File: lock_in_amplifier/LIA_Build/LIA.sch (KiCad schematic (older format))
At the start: 28 parts, among them J10 A IN COAX, J11 B IN, J12 POWER_IN, J13 A IN, J14 I IN COAX, J15 I IN, J16 TEST SIGNAL OUT, J18 TEST HIGH SIDE VALUE, J20 AMP OUT, J21 AMP OUT COAX, J22 CLK IN, J23 CLK IN COAX, J26 CLK OUT, J27 CLK OUT COAX, J30 DEMOD OUT - I, J31 DEMOD OUT I COAX, J32 DEMOD OUT Q COAX, J33 DEMOD OUT - Q, J9 B IN COAX

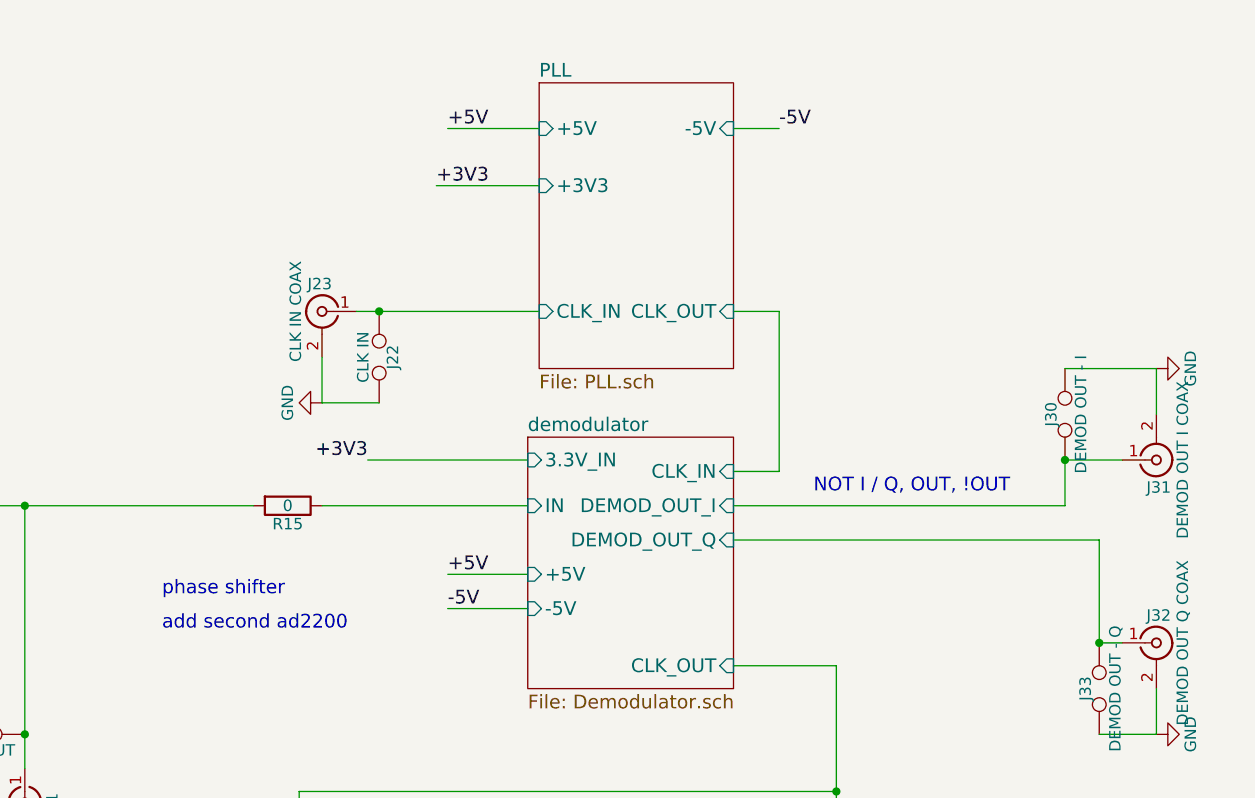
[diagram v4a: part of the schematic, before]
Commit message: Added quadrature demod, phase shift to pll
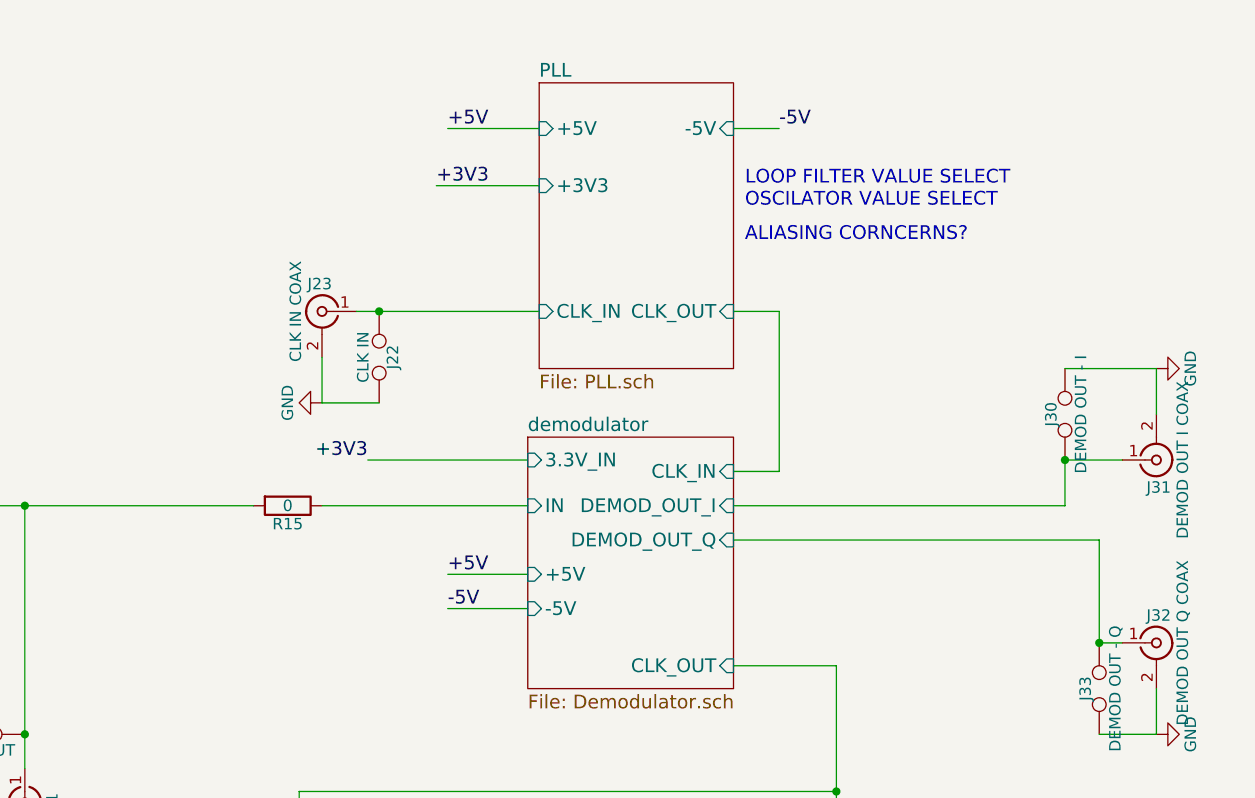
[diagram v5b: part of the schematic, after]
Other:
- note added: "ALIASING CORNCERNS?"
- note added: "LOOP FILTER VALUE SELECT\nOSCILATOR VALUE SELECT"
- note removed: "NOT I / Q, OUT, !OUT"
- note removed: "add second ad2200"
- note removed: "phase shifter"
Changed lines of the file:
@@
 $EndSheet
 $Comp
-L GND #PWR5
+L GND #PWR01
 U 1 1 5A1F9691
 P 2750 3650
-F 0 "#PWR5" H 2750 3400 50  0001 C CNN
+F 0 "#PWR01" H 2750 3400 50  0001 C CNN
 F 1 "GND" H 2750 3500 50  0000 C CNN
 F 2 "" H 2750 3650 50  0001 C CNN
@@
 $EndComp
 $Comp
-L GND #PWR3
+L GND #PWR02
 U 1 1 5A2003C9
 P 1500 2650
-F 0 "#PWR3" H 1500 2400 50  0001 C CNN
+F 0 "#PWR02" H 1500 2400 50  0001 C CNN
 F 1 "GND" H 1500 2500 50  0000 C CNN
 F 2 "" H 1500 2650 50  0001 C CNN
@@
 $EndComp
 $Comp
-L GND #PWR2
+L GND #PWR03
 U 1 1 5A2004F1
 P 1450 4150
-F 0 "#PWR2" H 1450 3900 50  0001 C CNN
+F 0 "#PWR03" H 1450 3900 50  0001 C CNN
 F 1 "GND" H 1450 4000 50  0000 C CNN
 F 2 "" H 1450 4150 50  0001 C CNN
@@
 $EndComp
 $Comp
-L GND #PWR1
+L GND #PWR04
 U 1 1 5A20072D
 P 950 3800
-F 0 "#PWR1" H 950 3550 50  0001 C CNN
+F 0 "#PWR04" H 950 3550 50  0001 C CNN
 F 1 "GND" H 950 3650 50  0000 C CNN
 F 2 "" H 950 3800 50  0001 C CNN
@@
 $EndComp
 $Comp
-L GND #PWR6
+L GND #PWR05
 U 1 1 5A203CBF
 P 4400 5150
-F 0 "#PWR6" H 4400 4900 50  0001 C CNN
+F 0 "#PWR05" H 4400 4900 50  0001 C CNN
 F 1 "GND" H 4400 5000 50  0000 C CNN
 F 2 "" H 4400 5150 50  0001 C CNN
@@
 $EndComp
 $Comp
-L GND #PWR7
+L GND #PWR06
 U 1 1 5A203EC2
 P 6100 3400
-F 0 "#PWR7" H 6100 3150 50  0001 C CNN
+F 0 "#PWR06" H 6100 3150 50  0001 C CNN
 F 1 "GND" H 6100 3250 50  0000 C CNN
 F 2 "" H 6100 3400 50  0001 C CNN
@@
 $EndComp
 $Comp
-L GND #PWR8
+L GND #PWR07
 U 1 1 5A203FFF
 P 7950 5800
-F 0 "#PWR8" H 7950 5550 50  0001 C CNN
+F 0 "#PWR07" H 7950 5550 50  0001 C CNN
 F 1 "GND" H 7950 5650 50  0000 C CNN
 F 2 "" H 7950 5800 50  0001 C CNN
@@
 $EndComp
 $Comp
-L GND #PWR9
+L GND #PWR08
 U 1 1 5A20451A
 P 9750 3250
-F 0 "#PWR9" H 9750 3000 50  0001 C CNN
+F 0 "#PWR08" H 9750 3000 50  0001 C CNN
 F 1 "GND" H 9750 3100 50  0000 C CNN
 F 2 "" H 9750 3250 50  0001 C CNN
@@
 $EndComp
 $Comp
-L GND #PWR10
+L GND #PWR09
 U 1 1 5A204657
 P 9750 4850
-F 0 "#PWR10" H 9750 4600 50  0001 C CNN
+F 0 "#PWR09" H 9750 4600 50  0001 C CNN
 F 1 "GND" H 9750 4700 50  0000 C CNN
 F 2 "" H 9750 4850 50  0001 C CNN
@@
 $EndComp
 $Comp
-L GND #PWR4
+L GND #PWR010
 U 1 1 5A212B2B
 P 1750 6850
-F 0 "#PWR4" H 1750 6600 50  0001 C CNN
+F 0 "#PWR010" H 1750 6600 50  0001 C CNN
 F 1 "GND" H 1750 6700 50  0000 C CNN
 F 2 "" H 1750 6850 50  0001 C CNN
@@
 Text Notes 7250 6600 0    60   ~ 0
 ADD SENSIBLE MCU OUT FOR EVENTUAL MICROCONTROLLER DESIGN
-Text Notes 5400 4250 0    60   ~ 0
-phase shifter
-Text Notes 8250 3800 0    60   ~ 0
-NOT I / Q, OUT, !OUT
-Text Notes 5400 4400 0    60   ~ 0
-add second ad2200
+Text Notes 7950 2550 0    60   ~ 0
+LOOP FILTER VALUE SELECT\nOSCILATOR VALUE SELECT
+Text Notes 7950 2700 0    60   ~ 0
+ALIASING CORNCERNS?
 $EndSCHEMATC

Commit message: pll finalized - misc cleanup - review candidate
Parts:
- added D10, D11, D12, D13, D9: BAT54S, TO_SOT_Packages_SMD:SOT-23, symbol D_Schottky_x2_Serial_AKC
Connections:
- net +3V3: now also D11.2 (K), D12.2 (K), D13.2 (K), D9.2 (K)
- net +5V: now also D10.2 (K)
- net -5V: now also D10.1 (A)
- net GND: now also D11.1 (A), D12.1 (A), D13.1 (A), D9.1 (A)
- net PLL/CLK_IN: now also D10.3 (common)
- net amplifiers/OUT: now also D9.3 (common)
- net demodulator/CLK_OUT: now also D11.3 (common)
- net demodulator/DEMOD_OUT_I: now also D13.3 (common)
- net demodulator/DEMOD_OUT_Q: now also D12.3 (common)
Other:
- note added: "CREATE AN OFFICIAL NOISE BUDGET\nEND TO END NOISE AND GAIN SIM\n"
- note added: "LOOP FILTER VALUE SELECT"
- note removed: "ADD SENSIBLE MCU OUT FOR EVENTUAL MICROCONTROLLER DESIGN"
- note removed: "ALIASING CORNCERNS?"
- note removed: "DFM TODO:\nRESISTOR COMP. CT. MINIMIZATION\nCONSIDER SMALLER PASSIVE PACKAGES (0603 OR 0402)\nMANUFACTURE TP. PLACEMENT.\nMANUFACTURE 0 OHM \nCHEAPER ALT. TO OP1177?\nADD ESD PROTECTION"
- note removed: "LOOP FILTER VALUE SELECT\nOSCILATOR VALUE SELECT"
- note removed: "MAJOR TODO:\nSELECT TRANSIMPEDANCE AMP\nAMPLIFIER NOISE TRADES - WRITEUP / VERIFY\nPLL SELECTION\nLINE FILTER DESIGN"
- note removed: "◦ Work noise budget!\n"
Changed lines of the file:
@@
 F9 "-5V" I L 7000 4300 60
 $EndSheet
-Text Notes 5050 1400 0    60   ~ 0
-	◦	Work noise budget!\n
+Text Notes 8700 800  0    60   ~ 0
+CREATE AN OFFICIAL NOISE BUDGET\nEND TO END NOISE AND GAIN SIM\n
 Text Notes 1650 4550 0    60   ~ 0
 layout notes:\nguard traces around A IN, BIN AND I IN\nlocate near to input connectors\nput 100mil headers under can outline
@@
 Text Notes 5550 6150 2    60   ~ 0
 GUARD TRACES AROUND HIGH IMPEDANCE PATHS
-Text Notes 5150 1200 0    60   ~ 0
-MAJOR TODO:\nSELECT TRANSIMPEDANCE AMP\nAMPLIFIER NOISE TRADES - WRITEUP / VERIFY\nPLL SELECTION\nLINE FILTER DESIGN
-Text Notes 7900 1250 0    60   ~ 0
-DFM TODO:\nRESISTOR COMP. CT. MINIMIZATION\nCONSIDER SMALLER PASSIVE PACKAGES (0603 OR 0402)\nMANUFACTURE TP. PLACEMENT.\nMANUFACTURE 0 OHM \nCHEAPER ALT. TO OP1177?\nADD ESD PROTECTION
 $Comp
 L SPDT S1
@@
 Wire Wire Line
 	6650 4150 7000 4150
-Text Notes 7250 6600 0    60   ~ 0
-ADD SENSIBLE MCU OUT FOR EVENTUAL MICROCONTROLLER DESIGN
 Text Notes 7950 2550 0    60   ~ 0
-LOOP FILTER VALUE SELECT\nOSCILATOR VALUE SELECT
-Text Notes 7950 2700 0    60   ~ 0
-ALIASING CORNCERNS?
+LOOP FILTER VALUE SELECT
+$Comp
+L D_Schottky_x2_Serial_AKC D9
+U 1 1 5A2A8E84
+P 4800 4600
+F 0 "D9" H 4850 4500 50  0000 C CNN
+F 1 "BAT54S" H 4800 4700 50  0000 C CNN
+F 2 "TO_SOT_Packages_SMD:SOT-23" H 4800 4600 50  0001 C CNN
+F 3 "" H 4800 4600 50  0001 C CNN
+	1    4800 4600
+	-1   0    0    1
+$EndComp
+Connection ~ 4800 4400
+$Comp
+L D_Schottky_x2_Serial_AKC D11
+U 1 1 5A2A90E7
+P 8350 4900
+F 0 "D11" H 8400 4800 50  0000 C CNN
+F 1 "BAT54S" H 8350 5000 50  0000 C CNN
+F 2 "TO_SOT_Packages_SMD:SOT-23" H 8350 4900 50  0001 C CNN
+F 3 "" H 8350 4900 50  0001 C CNN
+	1    8350 4900
+	-1   0    0    1
+$EndComp
+Connection ~ 8350 4700
+$Comp
+L D_Schottky_x2_Serial_AKC D12
+U 1 1 5A2A92A3
+P 8400 4000
+F 0 "D12" H 8450 3900 50  0000 C CNN
+F 1 "BAT54S" H 8400 4100 50  0000 C CNN
+F 2 "TO_SOT_Packages_SMD:SOT-23" H 8400 4000 50  0001 C CNN
+F 3 "" H 8400 4000 50  0001 C CNN
+	1    8400 4000
+	0    -1   -1   0
+$EndComp
+$Comp
+L D_Schottky_x2_Serial_AKC D13
+U 1 1 5A2A93F3
+P 8900 3850
+F 0 "D13" H 8950 3750 50  0000 C CNN
+F 1 "BAT54S" H 8900 3950 50  0000 C CNN
+F 2 "TO_SOT_Packages_SMD:SOT-23" H 8900 3850 50  0001 C CNN
+F 3 "" H 8900 3850 50  0001 C CNN
+	1    8900 3850
+	0    -1   -1   0
+$EndComp
+$Comp
+L D_Schottky_x2_Serial_AKC D10
+U 1 1 5A2A952B
+P 6650 3000
+F 0 "D10" H 6700 2900 50  0000 C CNN
+F 1 "BAT54S" H 6650 3100 50  0000 C CNN
+F 2 "TO_SOT_Packages_SMD:SOT-23" H 6650 3000 50  0001 C CNN
+F 3 "" H 6650 3000 50  0001 C CNN
+	1    6650 3000
+	0    -1   -1   0
+$EndComp
+Connection ~ 6850 3000
+$Comp
+L GND #PWR011
+U 1 1 5A2AB5C7
+P 5100 4600
+F 0 "#PWR011" H 5100 4350 50  0001 C CNN
+F 1 "GND" H 5100 4450 50  0000 C CNN
+F 2 "" H 5100 4600 50  0001 C CNN
+F 3 "" H 5100 4600 50  0001 C CNN
+	1    5100 4600
+	1    0    0    -1
+$EndComp
+$Comp
+L GND #PWR012
+U 1 1 5A2AB6F5
+P 8650 4900
+F 0 "#PWR012" H 8650 4650 50  0001 C CNN
+F 1 "GND" H 8650 4750 50  0000 C CNN
+F 2 "" H 8650 4900 50  0001 C CNN
+F 3 "" H 8650 4900 50  0001 C CNN
+	1    8650 4900
+	1    0    0    -1
+$EndComp
+$Comp
+L GND #PWR013
+U 1 1 5A2AB823
+P 8900 4150
+F 0 "#PWR013" H 8900 3900 50  0001 C CNN
+F 1 "GND" H 8900 4000 50  0000 C CNN
+F 2 "" H 8900 4150 50  0001 C CNN
+F 3 "" H 8900 4150 50  0001 C CNN
+	1    8900 4150
+	1    0    0    -1
+$EndComp
+$Comp
+L GND #PWR014
+U 1 1 5A2AB951
+P 8400 4300
+F 0 "#PWR014" H 8400 4050 50  0001 C CNN
+F 1 "GND" H 8400 4150 50  0000 C CNN
+F 2 "" H 8400 4300 50  0001 C CNN
+F 3 "" H 8400 4300 50  0001 C CNN
+	1    8400 4300
+	1    0    0    -1
+$EndComp
+Text Label 4500 4600 2    60   ~ 0
++3V3
+Text Label 8900 3550 2    60   ~ 0
++3V3
+Text Label 8400 3700 2    60   ~ 0
++3V3
+Text Label 8050 4900 2    60   ~ 0
++3V3
+Text Label 6650 2700 0    60   ~ 0
++5V
+Text Label 6650 3300 0    60   ~ 0
+-5V
+Connection ~ 8600 4000
+Connection ~ 9100 3850
 $EndSCHEMATC

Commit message: started LNA test board.
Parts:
- J12, S1: footprint (none) -> Pin_Headers:Pin_Header_Straight_1x03_Pitch2.54mm
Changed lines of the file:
@@
 F 0 "J12" H 1100 1600 50  0000 C CNN
 F 1 "POWER_IN" H 1100 1200 50  0000 C CNN
-F 2 "" H 1100 1400 50  0001 C CNN
+F 2 "Pin_Headers:Pin_Header_Straight_1x03_Pitch2.54mm" H 1100 1400 50  0001 C CNN
 F 3 "" H 1100 1400 50  0001 C CNN
 	1    1100 1400
@@
 F 0 "S1" H 1900 6450 50  0000 L CNN
 F 1 "TEST LOW VALUE SELECT" H 1750 6850 50  0000 L CNN
-F 2 "" H 2050 6700 50  0001 C CNN
+F 2 "Pin_Headers:Pin_Header_Straight_1x03_Pitch2.54mm" H 2050 6700 50  0001 C CNN
 F 3 "" H 2050 6700 50  0001 C CNN
 	1    2050 6650

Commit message: adressing comments - fets
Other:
- note added: "WILKINSON DEVIDER FOR DEMODS"
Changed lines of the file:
@@
 $EndSheet
 $Comp
-L GND #PWR01
+L GND #PWR5
 U 1 1 5A1F9691
 P 2750 3650
-F 0 "#PWR01" H 2750 3400 50  0001 C CNN
+F 0 "#PWR5" H 2750 3400 50  0001 C CNN
 F 1 "GND" H 2750 3500 50  0000 C CNN
 F 2 "" H 2750 3650 50  0001 C CNN
@@
 $EndComp
 $Comp
-L GND #PWR02
+L GND #PWR3
 U 1 1 5A2003C9
 P 1500 2650
-F 0 "#PWR02" H 1500 2400 50  0001 C CNN
+F 0 "#PWR3" H 1500 2400 50  0001 C CNN
 F 1 "GND" H 1500 2500 50  0000 C CNN
 F 2 "" H 1500 2650 50  0001 C CNN
@@
 $EndComp
 $Comp
-L GND #PWR03
+L GND #PWR2
 U 1 1 5A2004F1
 P 1450 4150
-F 0 "#PWR03" H 1450 3900 50  0001 C CNN
+F 0 "#PWR2" H 1450 3900 50  0001 C CNN
 F 1 "GND" H 1450 4000 50  0000 C CNN
 F 2 "" H 1450 4150 50  0001 C CNN
@@
 $EndComp
 $Comp
-L GND #PWR04
+L GND #PWR1
 U 1 1 5A20072D
 P 950 3800
-F 0 "#PWR04" H 950 3550 50  0001 C CNN
+F 0 "#PWR1" H 950 3550 50  0001 C CNN
 F 1 "GND" H 950 3650 50  0000 C CNN
 F 2 "" H 950 3800 50  0001 C CNN
@@
 $EndComp
 $Comp
-L GND #PWR05
+L GND #PWR6
 U 1 1 5A203CBF
 P 4400 5150
-F 0 "#PWR05" H 4400 4900 50  0001 C CNN
+F 0 "#PWR6" H 4400 4900 50  0001 C CNN
 F 1 "GND" H 4400 5000 50  0000 C CNN
 F 2 "" H 4400 5150 50  0001 C CNN
@@
 $EndComp
 $Comp
-L GND #PWR06
+L GND #PWR8
 U 1 1 5A203EC2
 P 6100 3400
-F 0 "#PWR06" H 6100 3150 50  0001 C CNN
+F 0 "#PWR8" H 6100 3150 50  0001 C CNN
 F 1 "GND" H 6100 3250 50  0000 C CNN
 F 2 "" H 6100 3400 50  0001 C CNN
@@
 $EndComp
 $Comp
-L GND #PWR07
+L GND #PWR9
 U 1 1 5A203FFF
 P 7950 5800
-F 0 "#PWR07" H 7950 5550 50  0001 C CNN
+F 0 "#PWR9" H 7950 5550 50  0001 C CNN
 F 1 "GND" H 7950 5650 50  0000 C CNN
 F 2 "" H 7950 5800 50  0001 C CNN
@@
 $EndComp
 $Comp
-L GND #PWR08
+L GND #PWR13
 U 1 1 5A20451A
 P 9750 3250
-F 0 "#PWR08" H 9750 3000 50  0001 C CNN
+F 0 "#PWR13" H 9750 3000 50  0001 C CNN
 F 1 "GND" H 9750 3100 50  0000 C CNN
 F 2 "" H 9750 3250 50  0001 C CNN
@@
 $EndComp
 $Comp
-L GND #PWR09
+L GND #PWR14
 U 1 1 5A204657
 P 9750 4850
-F 0 "#PWR09" H 9750 4600 50  0001 C CNN
+F 0 "#PWR14" H 9750 4600 50  0001 C CNN
 F 1 "GND" H 9750 4700 50  0000 C CNN
 F 2 "" H 9750 4850 50  0001 C CNN
@@
 $EndComp
 $Comp
-L GND #PWR010
+L GND #PWR4
 U 1 1 5A212B2B
 P 1750 6850
-F 0 "#PWR010" H 1750 6600 50  0001 C CNN
+F 0 "#PWR4" H 1750 6600 50  0001 C CNN
 F 1 "GND" H 1750 6700 50  0000 C CNN
 F 2 "" H 1750 6850 50  0001 C CNN
@@
 Connection ~ 6850 3000
 $Comp
-L GND #PWR011
+L GND #PWR7
 U 1 1 5A2AB5C7
 P 5100 4600
-F 0 "#PWR011" H 5100 4350 50  0001 C CNN
+F 0 "#PWR7" H 5100 4350 50  0001 C CNN
 F 1 "GND" H 5100 4450 50  0000 C CNN
 F 2 "" H 5100 4600 50  0001 C CNN
@@
 $EndComp
 $Comp
-L GND #PWR012
+L GND #PWR11
 U 1 1 5A2AB6F5
 P 8650 4900
-F 0 "#PWR012" H 8650 4650 50  0001 C CNN
+F 0 "#PWR11" H 8650 4650 50  0001 C CNN
 F 1 "GND" H 8650 4750 50  0000 C CNN
 F 2 "" H 8650 4900 50  0001 C CNN
@@
 $EndComp
 $Comp
-L GND #PWR013
+L GND #PWR12
 U 1 1 5A2AB823
 P 8900 4150
-F 0 "#PWR013" H 8900 3900 50  0001 C CNN
+F 0 "#PWR12" H 8900 3900 50  0001 C CNN
 F 1 "GND" H 8900 4000 50  0000 C CNN
 F 2 "" H 8900 4150 50  0001 C CNN
@@
 $EndComp
 $Comp
-L GND #PWR014
+L GND #PWR10
 U 1 1 5A2AB951
 P 8400 4300
-F 0 "#PWR014" H 8400 4050 50  0001 C CNN
+F 0 "#PWR10" H 8400 4050 50  0001 C CNN
 F 1 "GND" H 8400 4150 50  0000 C CNN
 F 2 "" H 8400 4300 50  0001 C CNN
@@
 Connection ~ 8600 4000
 Connection ~ 9100 3850
+Text Notes 4750 2250 0    60   ~ 0
+WILKINSON DEVIDER FOR DEMODS
 $EndSCHEMATC
